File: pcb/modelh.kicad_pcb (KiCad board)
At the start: 2 copper layers, 150 x 38 mm, 50 parts, among them J1 USB_C_Receptacle_USB2.0, J2 Conn_01x16, J3 Conn_01x12, J4 Conn_01x04, J5 Conn_02x03_Odd_Even, J6 Conn_02x05_Odd_Even, J7 Conn_01x05, J8 Conn_01x05, J9 Conn_01x05, SW1 SW_Push, U1 STM32F103C8Tx, U2 AMS1117-3.3, Y1 8MHz

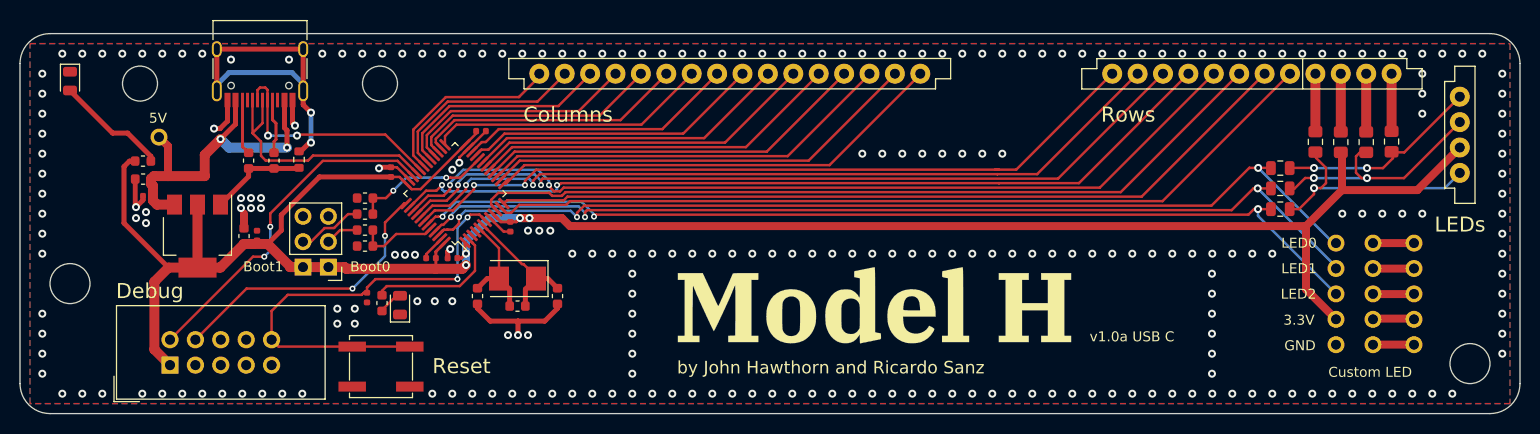
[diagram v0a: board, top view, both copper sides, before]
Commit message: Adds 3D files to repository
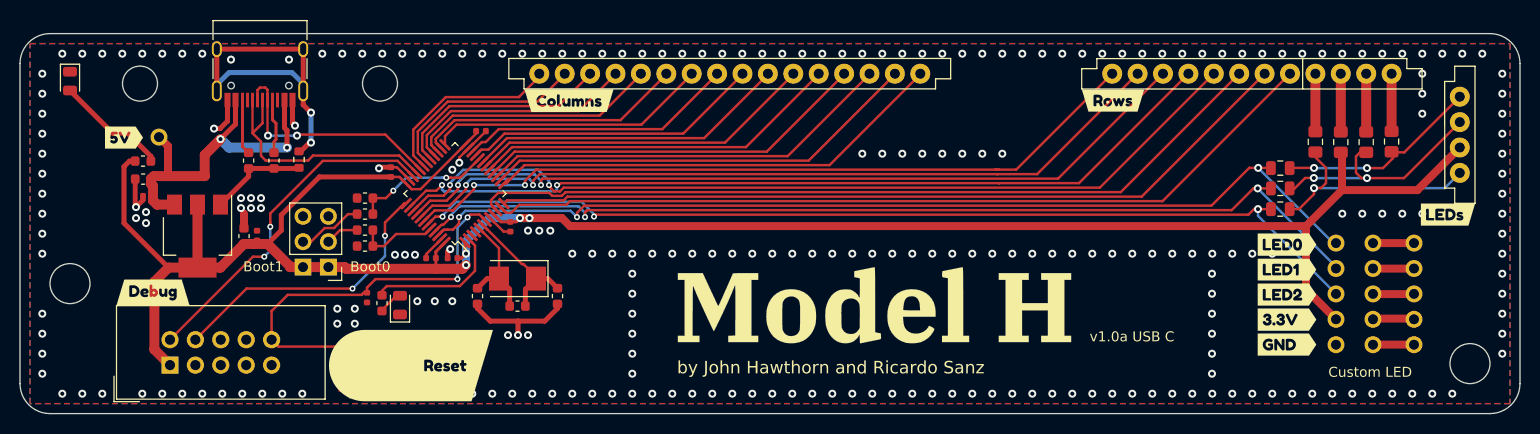
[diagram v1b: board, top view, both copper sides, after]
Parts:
- added kibuzzard-61E18CD3: G***, kibuzzard-61E18CD3, F.Cu at (119.7, 53.7)
- added kibuzzard-61E18CE3: G***, kibuzzard-61E18CE3, F.Cu at (174.1, 53.7)
- added kibuzzard-61E18F66: G***, kibuzzard-61E18F66, F.Cu at (103.9, 80.2)
- added kibuzzard-61E1917D: G***, kibuzzard-61E1917D, F.Cu at (78.1, 72.9)
- added kibuzzard-61E1928B: G***, kibuzzard-61E1928B, F.Cu at (207.6, 65.1)
- added kibuzzard-61E19345: G***, kibuzzard-61E19345, F.Cu at (191.5, 78.1)
- added kibuzzard-61E1934D: G***, kibuzzard-61E1934D, F.Cu at (191.5, 75.6)
- added kibuzzard-61E19354: G***, kibuzzard-61E19354, F.Cu at (191.5, 73.1)
- added kibuzzard-61E1935A: G***, kibuzzard-61E1935A, F.Cu at (191.5, 70.6)
- added kibuzzard-61E19361: G***, kibuzzard-61E19361, F.Cu at (191.5, 68.1)
- added kibuzzard-61E19404: G***, kibuzzard-61E19404, F.Cu at (75.2, 57.4)
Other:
- board text removed: "3.3V"
- board text removed: "5V"
- board text removed: "Columns"
- board text removed: "Debug"
- board text removed: "GND"
- board text removed: "LED0"
- board text removed: "LED1"
- board text removed: "LED2"
- board text removed: "LEDs"
- board text removed: "Reset"
- board text removed: "Rows"

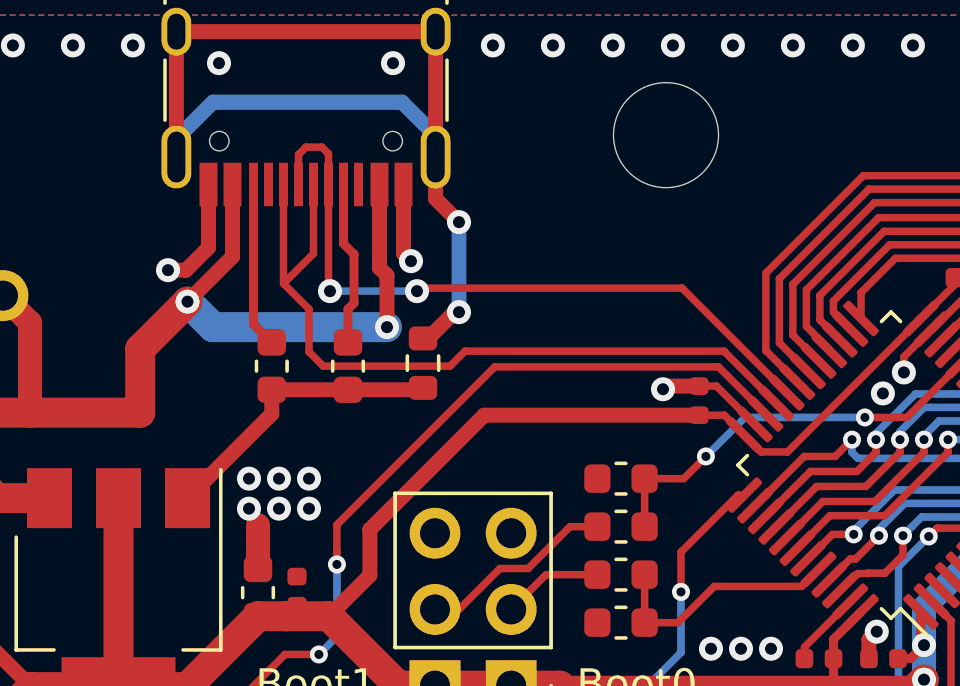
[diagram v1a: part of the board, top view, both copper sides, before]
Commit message: Renames a few components
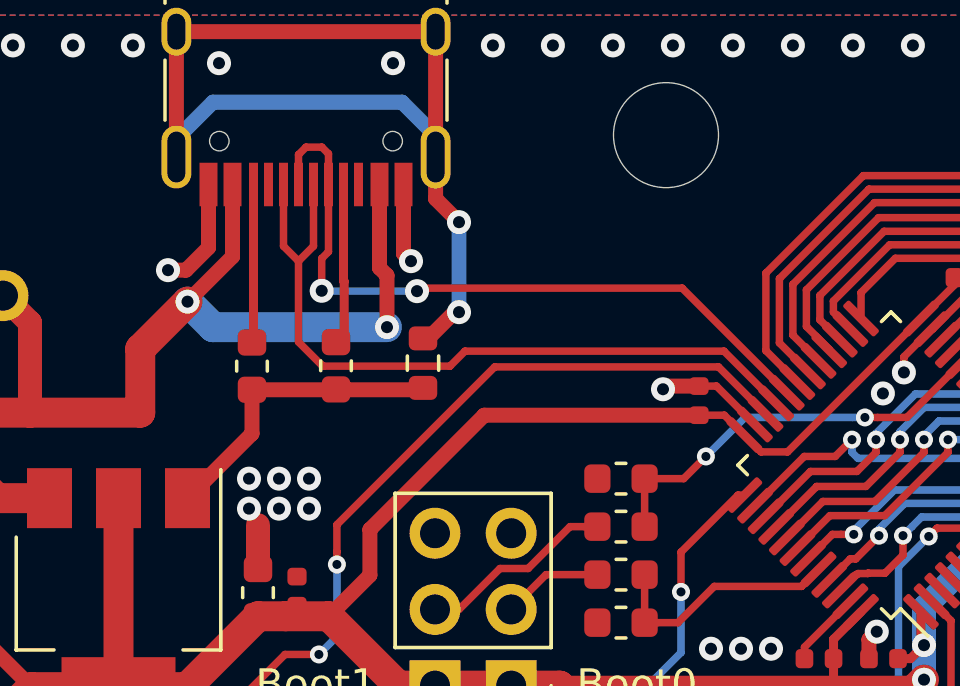
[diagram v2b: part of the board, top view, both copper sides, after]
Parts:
- U1: value STM32F103C8Tx -> GD32F103C8T6
- USB_C1: renamed from J1; value USB_C_Receptacle_USB2.0 -> TYPE-C-31-M-12
- moved R4 0.66 mm to (87.0, 59.7)
- moved R3 0.40 mm to (89.8, 59.7)
- renumbered J2 to Columns1, J6 to Debug1, J4 to LEDs1, J3 to Rows1, J5 to boot_selector1, J8 to custom_leds_A1, J9 to custom_leds_B1, J7 to custom_leds_C1

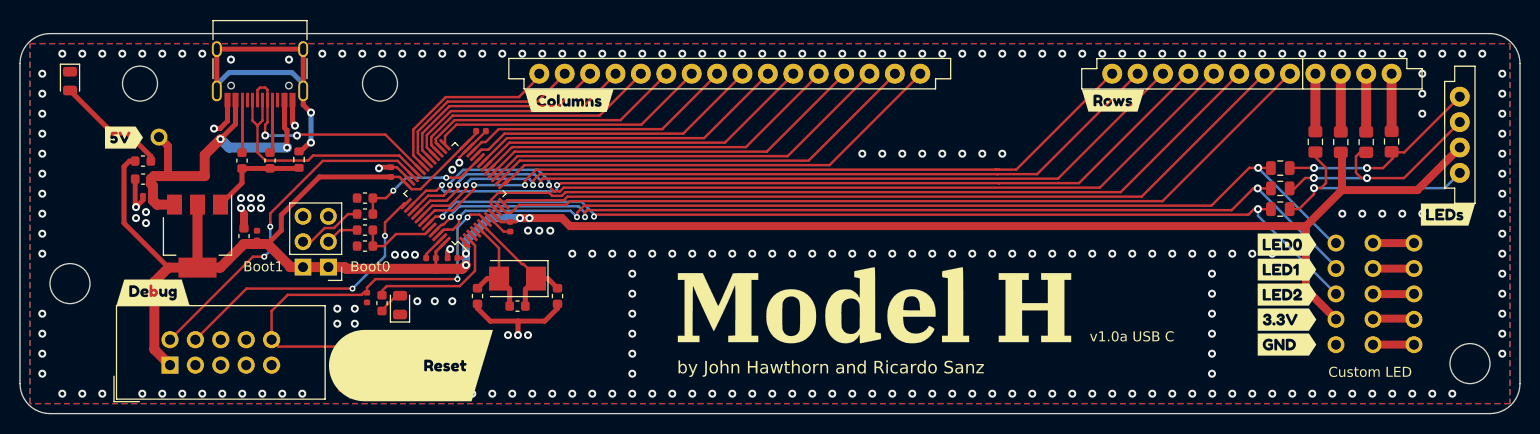
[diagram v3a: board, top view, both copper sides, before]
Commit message: Updates TE connectors footprints
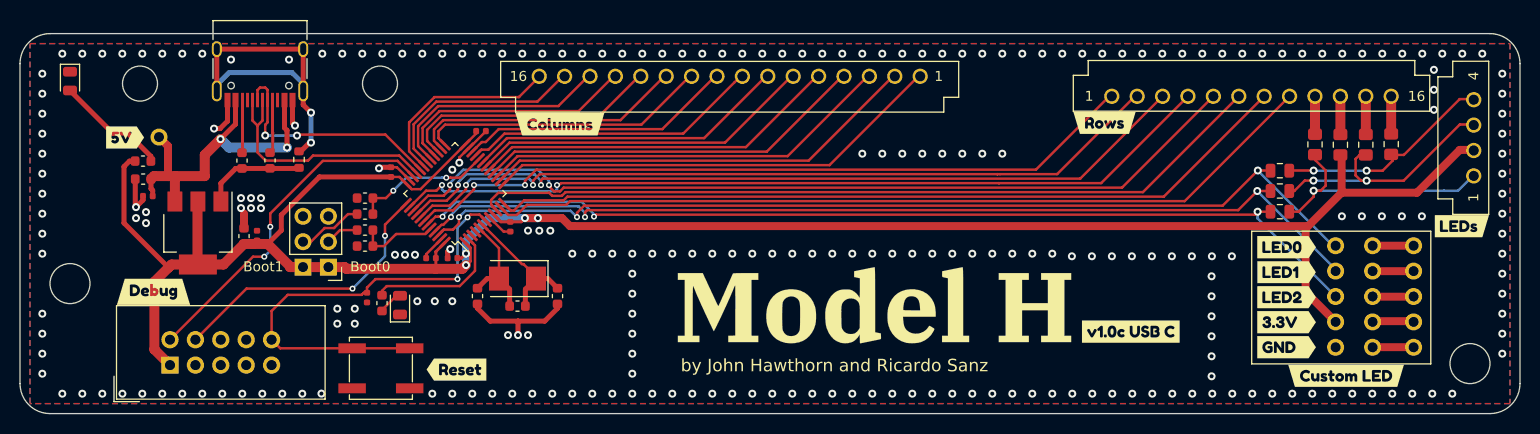
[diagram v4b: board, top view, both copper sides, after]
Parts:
- removed kibuzzard-61E18F66: G***, kibuzzard-61E18F66
- added kibuzzard-61E67D4F: G***, kibuzzard-61E67D4F, F.Cu at (108.4, 80.6)
- added kibuzzard-61E6F38C: G***, kibuzzard-61E6F38C, F.Cu at (197.4, 81.2)
- added kibuzzard-61E6F754: G***, kibuzzard-61E6F754, F.Cu at (175.8, 76.8)
- Columns1: value Conn_01x16 -> 6-520315-6; footprint modelh:ModelH-triomate-cols16 -> footprints:CONN_6-520315-6_TYC
- LEDs1: value Conn_01x04 -> 5-520315-4; footprint modelh:ModelH-tripmate-leds4 -> footprints:CONN_5-520315-4_TYC
- Rows1: value Conn_01x12 -> 6-520315-2; footprint modelh:ModelH-triomate-rows12 -> footprints:CONN_6-520315-2_TYC
- moved Columns1 19.0 mm to (154.8, 51.3), turned to 180 degrees
- moved Rows1 14.2 mm to (173.9, 53.3)
- moved LEDs1 4.34 mm to (210.1, 61.2), turned to 90 degrees
- moved kibuzzard-61E18CD3 2.52 mm to (118.8, 56.0)
- moved kibuzzard-61E18CE3 2.39 mm to (173.2, 55.9)
- moved kibuzzard-61E1928B 1.81 mm to (209.0, 66.2)
- moved U2 0.31 mm to (82.6, 66.9)
- moved R15 0.26 mm to (201.9, 58.0)
- moved R7 0.26 mm to (190.8, 60.7)
- moved R12 0.26 mm to (194.3, 58.1)
- moved custom_leds_A1 0.26 mm to (196.3, 68.2)
- moved custom_leds_B1 0.26 mm to (200.0, 68.2)
- moved custom_leds_C1 0.26 mm to (204.1, 68.2)
- moved R8 0.26 mm to (190.8, 62.7)
- moved R13 0.26 mm to (196.8, 58.1)
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- renumbered REF** to HOLE1, REF** to HOLE2, REF** to HOLE3, REF** to HOLE4, G*** to MODELH_LOGO
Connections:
- Columns1 pad 1: col0 -> col15
- Columns1 pad 10: col9 -> col6
- Columns1 pad 11: col10 -> col5
- Columns1 pad 12: col11 -> col4
- Columns1 pad 13: col12 -> col3
- Columns1 pad 14: col13 -> col2
- Columns1 pad 15: col14 -> col1
- Columns1 pad 16: col15 -> col0
- Columns1 pad 2: col1 -> col14
- Columns1 pad 3: col2 -> col13
- Columns1 pad 4: col3 -> col12
- Columns1 pad 5: col4 -> col11
- Columns1 pad 6: col5 -> col10
- Columns1 pad 7: col6 -> col9
- Columns1 pad 8: col7 -> col8
- Columns1 pad 9: col8 -> col7
- LEDs1 pad 2: Net-(LEDs1-Pad2) -> +3V3
- LEDs1 pad 3: +3V3 -> Net-(LEDs1-Pad3)
- R12 pad 2: Net-(LEDs1-Pad4) -> Net-(LEDs1-Pad1)
- R14 pad 2: Net-(LEDs1-Pad2) -> Net-(LEDs1-Pad3)
- R15 pad 2: Net-(LEDs1-Pad1) -> Net-(LEDs1-Pad4)
- R7 pad 1: Net-(LEDs1-Pad1) -> Net-(LEDs1-Pad4)
- R8 pad 1: Net-(LEDs1-Pad2) -> Net-(LEDs1-Pad3)
- R9 pad 1: Net-(LEDs1-Pad4) -> Net-(LEDs1-Pad1)
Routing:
- net Net-(LEDs1-Pad3): track 0.00 -> 25.4 mm, vias 0 -> 2
- net Net-(LEDs1-Pad2): track 24.0 -> 0.00 mm, vias 2 -> 0
- net Net-(LEDs1-Pad1): track 20.5 -> 25.2 mm, vias 2 -> 1
- net +3V3: track 220.1 -> 223.9 mm
- net Net-(R15-Pad1): track 5.76 -> 3.76 mm
- net Net-(R14-Pad1): track 5.81 -> 3.82 mm
- net Net-(R12-Pad1): track 5.79 -> 3.79 mm
- net Net-(R13-Pad1): track 5.81 -> 3.82 mm
- net Net-(LEDs1-Pad4): track 23.8 -> 21.9 mm, vias 1 -> 2
- net row0: track 75.8 -> 74.6 mm
- net col6: track 28.1 -> 29.3 mm
- net col4: track 25.3 -> 26.3 mm
- net col3: track 23.7 -> 24.7 mm
- net col2: track 22.1 -> 23.2 mm
- net col1: track 20.6 -> 21.6 mm
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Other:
- board text removed: "Custom LED"
- board text removed: "v1.0a USB C"

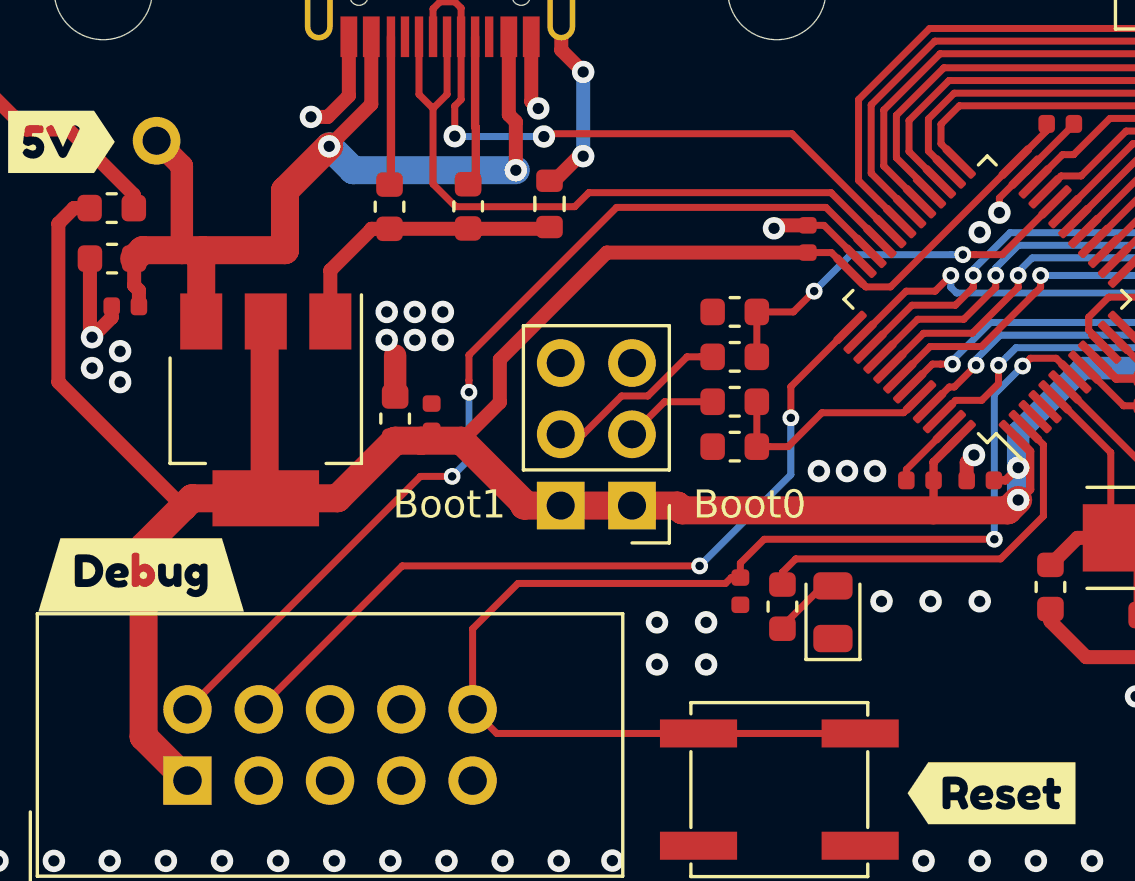
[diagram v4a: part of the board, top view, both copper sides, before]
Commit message: Updates silkscreen to make clear boot selector
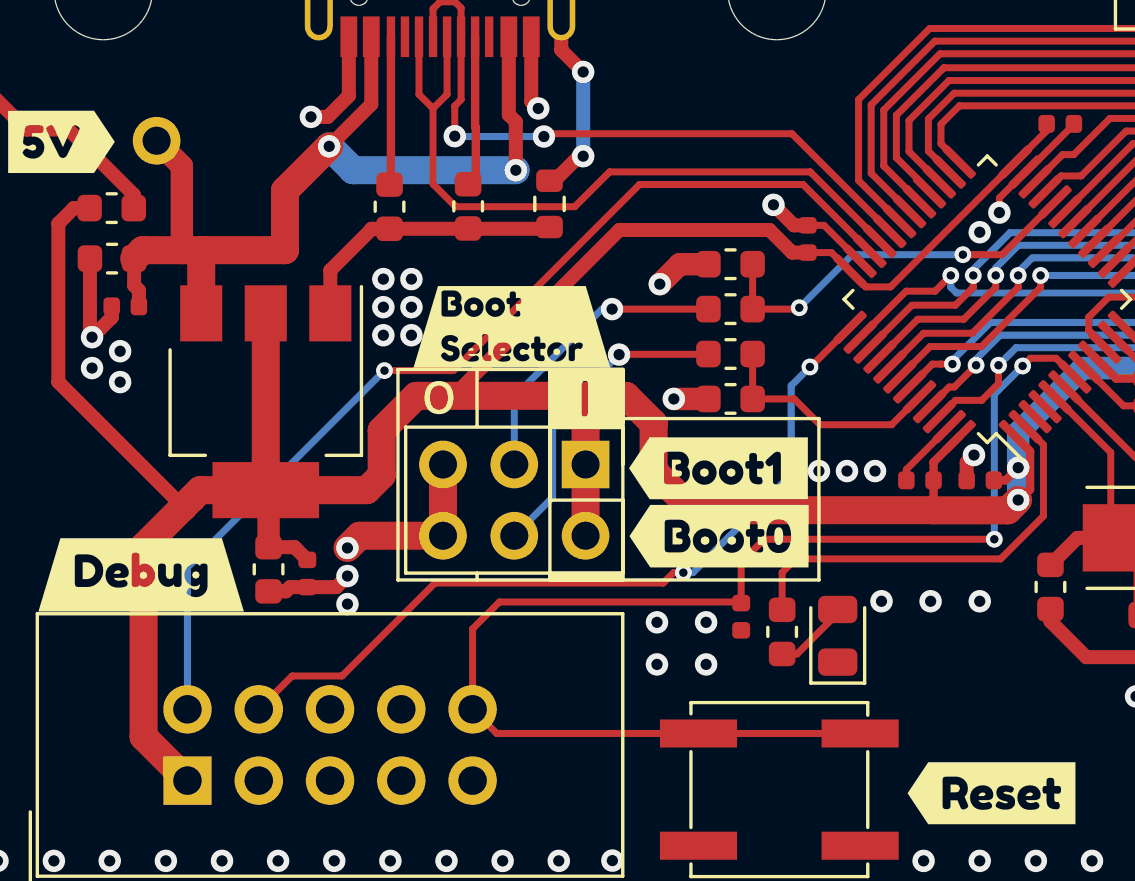
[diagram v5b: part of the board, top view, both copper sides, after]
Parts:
- added kibuzzard-61E8358A: G***, kibuzzard-61E8358A, F.Cu at (98.7, 71.4)
- added kibuzzard-61E83597: G***, kibuzzard-61E83597, F.Cu at (98.7, 69.0)
- added kibuzzard-61E83ADE: G***, kibuzzard-61E83ADE, F.Cu at (91.3, 64.0)
- added kibuzzard-61E846DB: G***, kibuzzard-61E846DB, F.Cu at (93.9, 66.5)
- moved C4 7.12 mm to (84.0, 72.8), turned to -90 degrees
- moved C3 7.01 mm to (82.7, 72.6), turned to -90 degrees
- moved boot_selector1 2.21 mm to (94.0, 68.9), turned to -90 degrees
- moved R10 1.71 mm to (99.1, 63.3)
- moved R5 1.71 mm to (99.1, 64.9)
- moved R18 1.71 mm to (99.1, 61.7)
- moved R17 1.71 mm to (99.1, 66.5)
- moved C9 0.91 mm to (99.5, 74.3)
- moved R2 0.90 mm to (101.0, 74.8)
- moved LED2 0.86 mm to (102.9, 75.0)
- moved U2 0.29 mm to (82.6, 66.6)
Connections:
- R10 pad 2: Net-(R10-Pad2) -> Net-(boot_selector1-Pad3)
- boot_selector1 pad 3: Net-(R5-Pad1) -> Net-(boot_selector1-Pad3)
- boot_selector1 pad 4: Net-(R10-Pad2) -> Net-(R5-Pad1)
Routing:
- net GND: track 47.6 -> 58.8 mm, vias 258 -> 263
- net +3V3: track 223.9 -> 234.8 mm
- net Net-(boot_selector1-Pad3): track 0.00 -> 10.5 mm, vias 0 -> 1
- net Net-(R5-Pad1): track 3.35 -> 11.2 mm, vias 0 -> 1
- net Net-(R10-Pad2): track 6.56 -> 0.00 mm
- net SWDIO: track 34.6 -> 36.0 mm, vias 2 -> 1
- net STATUSLED: track 14.0 -> 14.9 mm
- net D+: track 25.4 -> 26.0 mm
- net nRST: track 46.1 -> 46.7 mm
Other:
- board text added: "o"
- board text removed: "Boot0"
- board text removed: "Boot1"

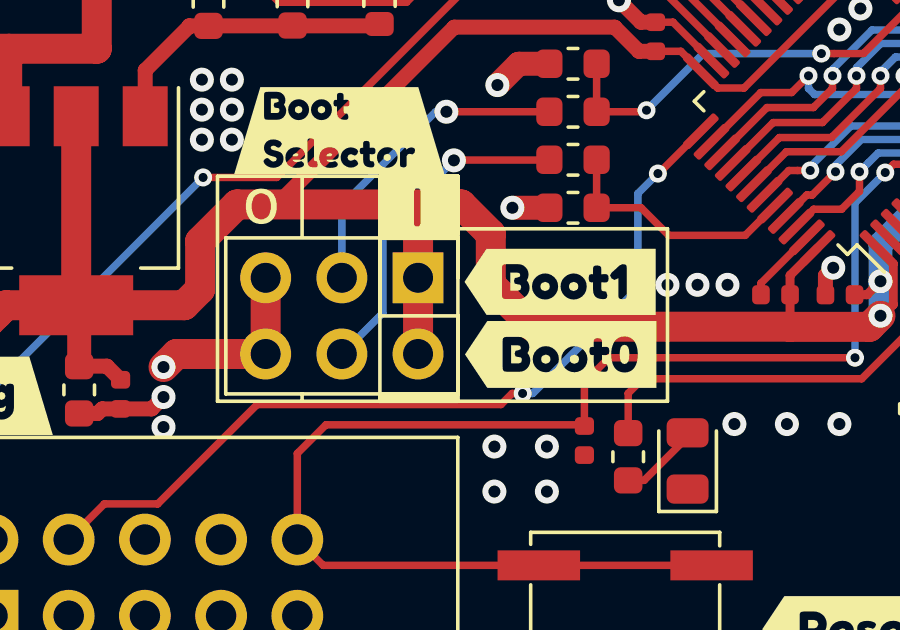
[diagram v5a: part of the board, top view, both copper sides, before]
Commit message: Adjust footprints
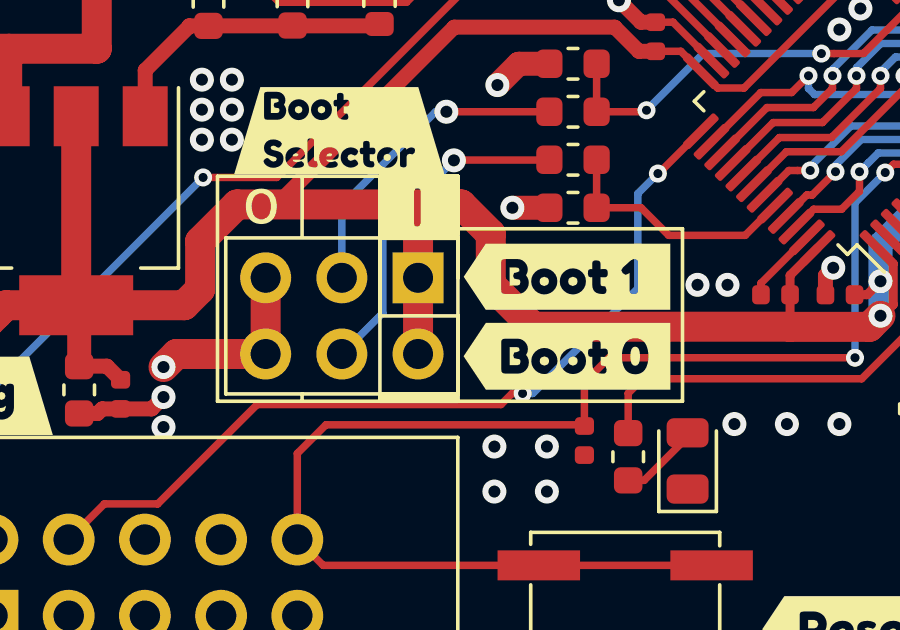
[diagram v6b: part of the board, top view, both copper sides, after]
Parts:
- removed kibuzzard-61E8358A: G***, kibuzzard-61E8358A
- removed kibuzzard-61E83597: G***, kibuzzard-61E83597
- added kibuzzard-61E84BB4: G***, kibuzzard-61E84BB4, F.Cu at (98.9, 68.8)
- added kibuzzard-61E84BBD: G***, kibuzzard-61E84BBD, F.Cu at (98.9, 71.5)
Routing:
- net GND: vias 263 -> 262
